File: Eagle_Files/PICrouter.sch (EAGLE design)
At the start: 44 parts, among them IC1 PIC32MX675F512H, IC2 48M033F, J1 POWER_JACK, Q1 20MHz, Q2 BSS84, X2 USB_B

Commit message: Released PICrouter schematic and board v0.4.
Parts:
- added C14, C16, C17, C18, C20, C21, C22, C23, C24: (no value), rcl:C-EUC2012
- added C15, C19: 10uF, rcl:CPOL-USC
- added IC3: DP83848, national-semiconductor:DP83848
- added J2: (no value), pulse_j0011:J0011
- added QG1: SM77H, crystal:SM77H
- added R11, R12, R13, R14: 49.9, SparkFun:RESISTOR0603-RES
- added R15: 4.87k, SparkFun:RESISTOR0603-RES
- added R16, R17, R22: 2.2k, SparkFun:RESISTOR0603-RES
- added R18, R19, R2, R20, R23, R24: 33, SparkFun:RESISTOR0603-RES
- added R21, R25: 1.5k, SparkFun:RESISTOR0603-RES
- added R26, R27: 330, SparkFun:RESISTOR0603-RES
- Q1: device special:XTAL/S -> crystal:CRYSTALCTS406
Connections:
- new net ECRSDV: IC1.ERXDV/ECRSDV/PMD2/RE2, IC3.CRS
- new net EINT: IC1.ECRS/AEREFCLK/IC4/PMCS1/PMA14/INT4/RD11, IC3.PWRDN_INTN, R21.1
- new net EMDC: IC1.AN15/EMDC/AEMDC/OCFB/PMALL/PMA0/CN12/RB15, IC3.MDC
- new net EMDIO: IC1.EMDIO/AEMDIO/SCK3/U4TX/U1RTS/OC2/RD1, IC3.MDIO, R25.2
- new net EREFCLK: IC1.ERXCLK/EREFCLK/PMD3RE3, IC3.X1, R2.2
- new net ERXD0: IC1.ERXD0/PMD1/RE1, R23.1
- new net ERXD1: IC1.ERXD1/PMD0/RE0, R24.1
- new net ERXERR: IC1.ERXERR/PMD4/RE4, IC3.RX_ER
- new net ETXD0: IC1.ETXD0/PMD6/RE6, R19.1
- new net ETXD1: IC1.ETXD1/PMD7/RE7, R20.1
- new net ETXEN: IC1.ETXEN/PMD5/RE5, R18.1
- new net LED_ACT: IC3.LED_ACTCOL, R27.1
- new net LED_LINK: IC3.LED_LNK, R26.1
- new net N$47: IC3.IP_PH_P, R16.1
- new net N$48: IC3.IP_PH_M, R17.1
- new net N$49: IC3.RX_DV, R22.2
- new net N$52: IC3.TXD_1, R20.2
- new net N$53: IC3.TXD_0, R19.2
- new net N$54: IC3.TX_EN, R18.2
- new net N$55: J2.LA, R26.2
- new net N$56: IC3.RXD_0, R23.2
- new net N$57: IC3.RXD_1, R24.2
- new net N$58: QG1.OUT, R2.1
- new net N$62: J2.RA, R27.2
- new net N$9: IC3.VREF, R15.1
- new net PFBOUT: C14.1, C18.1, C19.+, C20.1, IC3.ANA18VDD, IC3.CORE_VDD, IC3.REG_OUT
- new net RDM: IC3.TPRDM, J2.RD-, R11.1
- new net RDP: IC3.TPRDP, J2.RD+, R12.1
- new net TDM: IC3.TPTDM, J2.TD-, R13.1
- new net TDP: IC3.TPTDP, J2.TD+, R14.1
- net GND: now also C14.2, C15.-, C16.2, C17.2, C18.2, C19.-, C20.2, C21.2, C22.2, C23.2, C24.2, IC3.ANA18VSS, IC3.CDVSS, IC3.CORE_VSS, IC3.IO_VSS1, IC3.IO_VSS2, IC3.TXD_3, J2.CGND, J2.LC, J2.RC, J2.S1, J2.S2, QG1.GND, R15.2
- net N$17: now also IC1.ECOL/AECRSDV/SCL1/IC3/PMCS2/PMA15/INT3/RD10; no longer IC1.AN15/EMDC/AEMDC/OCFB/PMALL/PMA0/CN12/RB15
- net VDD: now also C15.+, C16.1, C17.1, C21.1, C22.1, C23.1, C24.1, IC3.ANA33VDD, IC3.IO_VDD1, IC3.IO_VDD2, J2.RCT, J2.TCT, QG1.VCC, R11.2, R12.2, R13.2, R14.2, R16.2, R17.2, R21.2, R22.1, R25.1
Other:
- note added: "03/24/2012"
- note added: "PICrouter v0.5"
- note removed: "09/06/2011"
- note removed: "PICrouter v0.3"

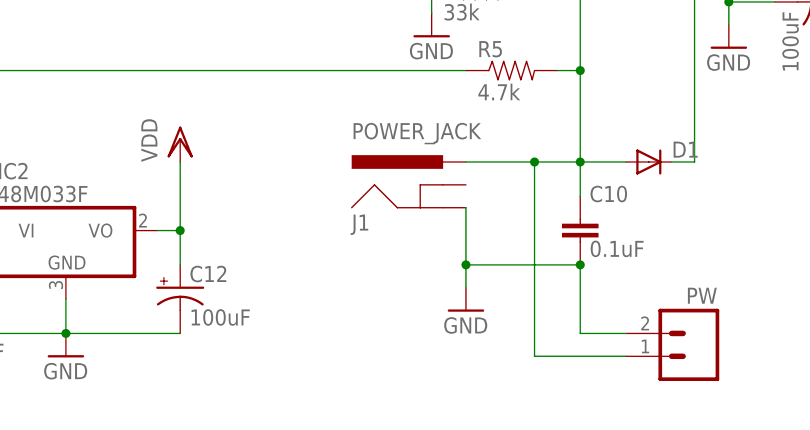
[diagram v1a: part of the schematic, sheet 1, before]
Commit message: Released PICrouter schematic and board v0.6.
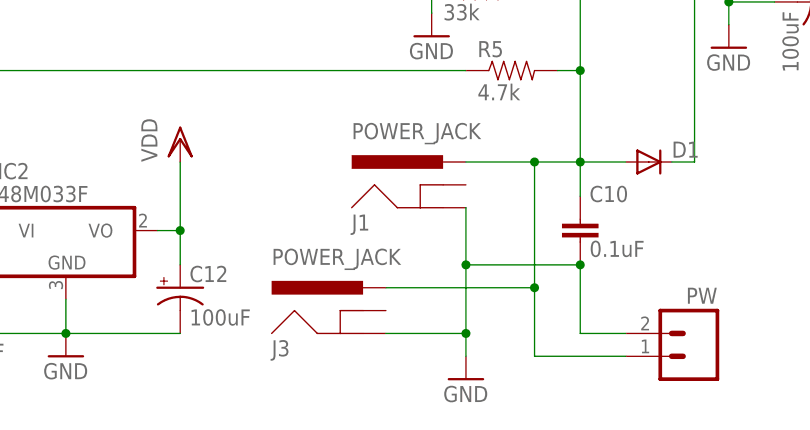
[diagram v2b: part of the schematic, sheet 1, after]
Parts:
- added J3: POWER_JACK, SparkFun:POWER_JACKPTH_LOCK
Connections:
- net GND: now also J3.GND
- net N$46: now also J3.PWR
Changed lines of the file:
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@@
 <part name="R26" library="SparkFun" deviceset="RESISTOR" device="0603-RES" value="330"/>
 <part name="R27" library="SparkFun" deviceset="RESISTOR" device="0603-RES" value="330"/>
+<part name="J3" library="SparkFun" deviceset="POWER_JACK" device="PTH_LOCK" value="POWER_JACK"/>
 </parts>
 <sheets>
@@
 </instance>
 <instance part="C13" gate="G$1" x="199.39" y="49.53" rot="R270"/>
-<instance part="GND10" gate="1" x="160.02" y="15.24"/>
+<instance part="GND10" gate="1" x="160.02" y="7.62"/>
 <instance part="D1" gate="G$1" x="180.34" y="31.75"/>
 <instance part="D2" gate="G$1" x="180.34" y="58.42"/>
@@
 <instance part="C9" gate="G$1" x="207.01" y="133.35"/>
 <instance part="GND19" gate="1" x="212.09" y="138.43" rot="R90"/>
+<instance part="J3" gate="G$1" x="148.59" y="10.16"/>
 </instances>
 <busses>
@@
 <segment>
 <wire x1="160.02" y1="26.67" x2="160.02" y2="20.32" width="0.1524" layer="91"/>
-<wire x1="160.02" y1="20.32" x2="160.02" y2="17.78" width="0.1524" layer="91"/>
+<wire x1="160.02" y1="20.32" x2="160.02" y2="12.7" width="0.1524" layer="91"/>
+<wire x1="160.02" y1="12.7" x2="160.02" y2="10.16" width="0.1524" layer="91"/>
 <wire x1="172.72" y1="20.32" x2="160.02" y2="20.32" width="0.1524" layer="91"/>
 <wire x1="177.8" y1="12.7" x2="172.72" y2="12.7" width="0.1524" layer="91"/>
@@
 <pinref part="C10" gate="G$1" pin="2"/>
 <pinref part="PW" gate="G$1" pin="2"/>
+<pinref part="J3" gate="G$1" pin="GND"/>
+<wire x1="151.13" y1="12.7" x2="160.02" y2="12.7" width="0.1524" layer="91"/>
+<junction x="160.02" y="12.7"/>
 </segment>
 <segment>
@@
 <segment>
 <wire x1="177.8" y1="10.16" x2="167.64" y2="10.16" width="0.1524" layer="91"/>
-<wire x1="167.64" y1="10.16" x2="167.64" y2="31.75" width="0.1524" layer="91"/>
+<wire x1="167.64" y1="10.16" x2="167.64" y2="17.78" width="0.1524" layer="91"/>
+<wire x1="167.64" y1="17.78" x2="167.64" y2="31.75" width="0.1524" layer="91"/>
 <wire x1="166.37" y1="50.8" x2="167.64" y2="50.8" width="0.1524" layer="91"/>
 <wire x1="167.64" y1="50.8" x2="167.64" y2="53.34" width="0.1524" layer="91"/>
@@
 <pinref part="J1" gate="G$1" pin="PWR"/>
 <pinref part="R5" gate="G$1" pin="2"/>
-</segment>
-</net>
+<pinref part="J3" gate="G$1" pin="PWR"/>
+<wire x1="151.13" y1="17.78" x2="167.64" y2="17.78" width="0.1524" layer="91"/>
+<junction x="167.64" y="17.78"/>
+</segment>
+</net>

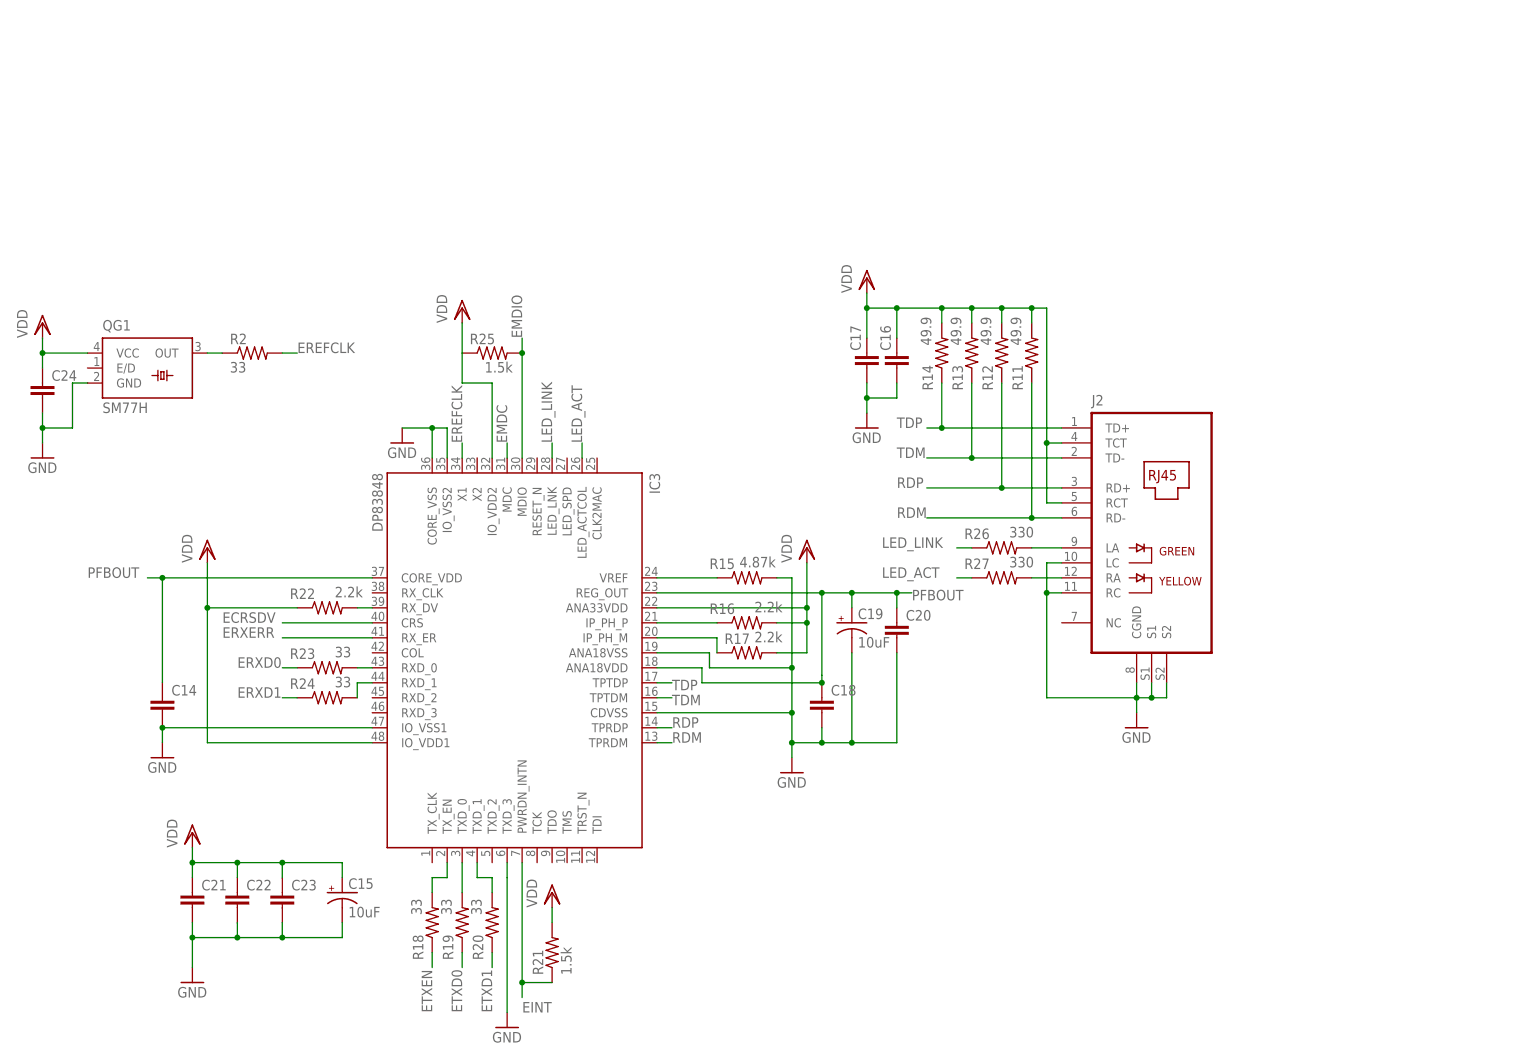
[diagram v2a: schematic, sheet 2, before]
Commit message: Released PICrouter schematic and board v0.7.
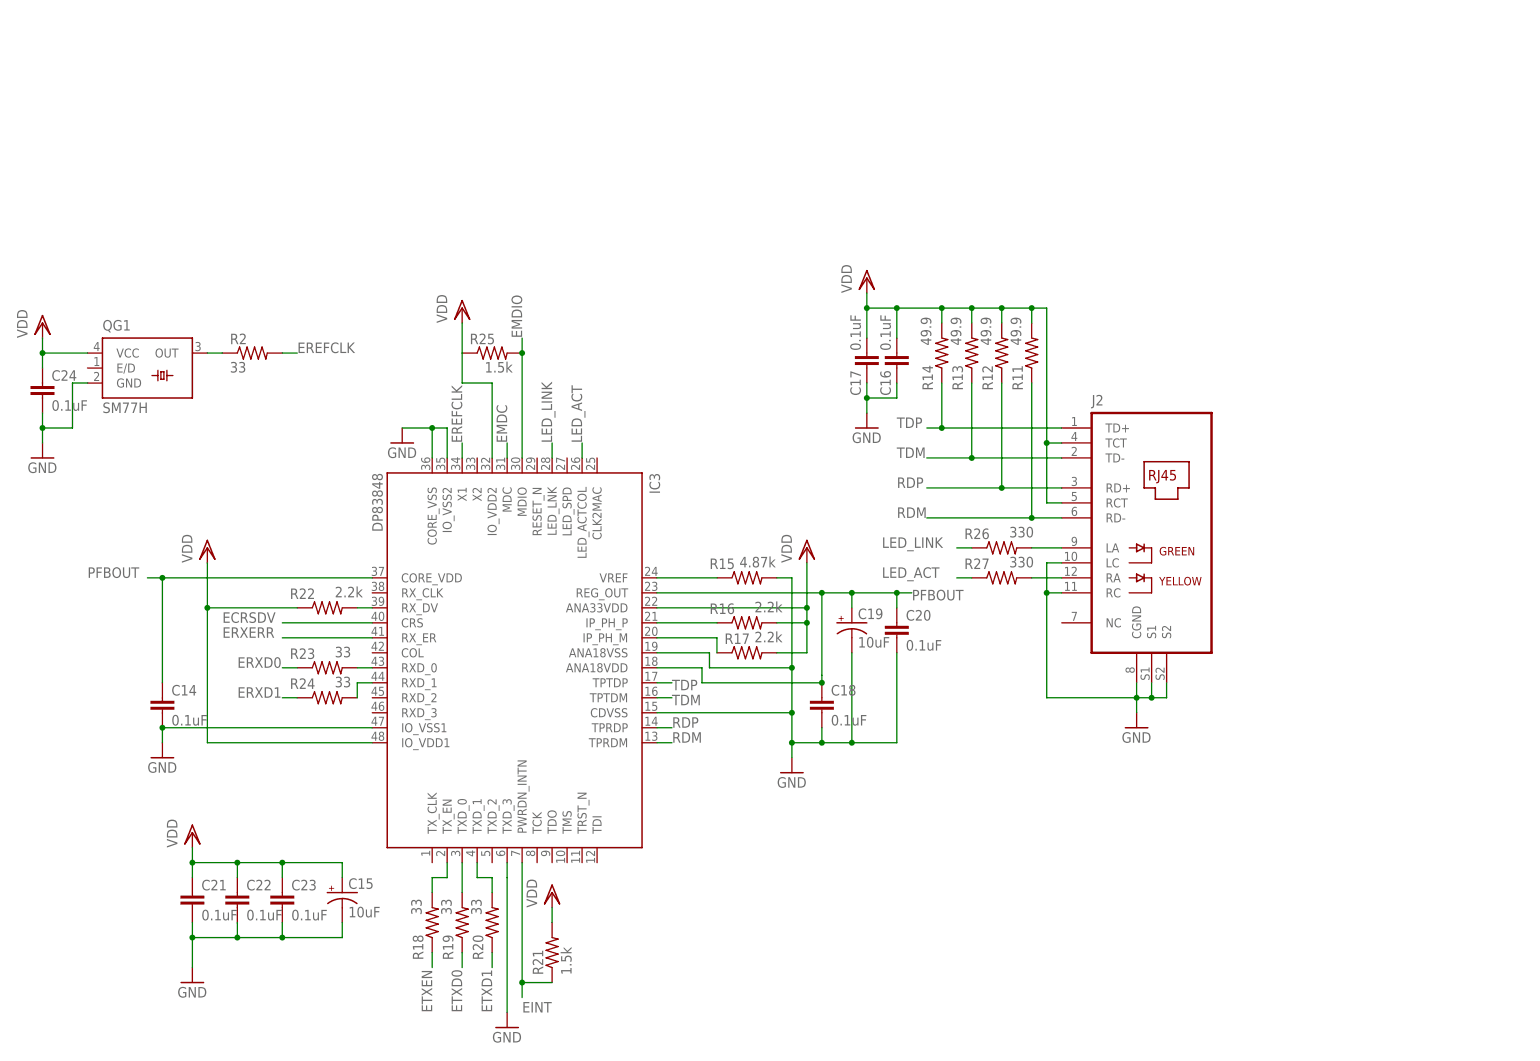
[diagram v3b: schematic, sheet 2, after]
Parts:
- C14, C16, C17, C18, C20, C21, C22, C23, C24: value (none) -> 0.1uF
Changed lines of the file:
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@@
 <setting verticaltext="up"/>
 </settings>
-<grid distance="0.05" unitdist="inch" unit="inch" style="lines" multiple="1" display="no" altdistance="0.01" altunitdist="inch" altunit="inch"/>
+<grid distance="0.1" unitdist="inch" unit="inch" style="lines" multiple="1" display="no" altdistance="0.01" altunitdist="inch" altunit="inch"/>
 <layers>
 <layer number="1" name="Top" color="4" fill="1" visible="no" active="no"/>
@@
 <part name="VDD10" library="supply1" deviceset="VDD" device=""/>
 <part name="GND20" library="supply1" deviceset="GND" device=""/>
-<part name="C14" library="rcl" deviceset="C-EU" device="C2012"/>
+<part name="C14" library="rcl" deviceset="C-EU" device="C2012" value="0.1uF"/>
 <part name="C15" library="rcl" deviceset="CPOL-US" device="C" value="10uF"/>
 <part name="J2" library="pulse_j0011" deviceset="J0011" device=""/>
@@
 <part name="R14" library="SparkFun" deviceset="RESISTOR" device="0603-RES" value="49.9"/>
 <part name="VDD11" library="supply1" deviceset="VDD" device=""/>
-<part name="C16" library="rcl" deviceset="C-EU" device="C2012"/>
-<part name="C17" library="rcl" deviceset="C-EU" device="C2012"/>
+<part name="C16" library="rcl" deviceset="C-EU" device="C2012" value="0.1uF"/>
+<part name="C17" library="rcl" deviceset="C-EU" device="C2012" value="0.1uF"/>
 <part name="GND21" library="supply1" deviceset="GND" device=""/>
 <part name="GND22" library="supply1" deviceset="GND" device=""/>
@@
 <part name="GND23" library="supply1" deviceset="GND" device=""/>
 <part name="VDD12" library="supply1" deviceset="VDD" device=""/>
-<part name="C18" library="rcl" deviceset="C-EU" device="C2012"/>
+<part name="C18" library="rcl" deviceset="C-EU" device="C2012" value="0.1uF"/>
 <part name="C19" library="rcl" deviceset="CPOL-US" device="C" value="10uF"/>
-<part name="C20" library="rcl" deviceset="C-EU" device="C2012"/>
+<part name="C20" library="rcl" deviceset="C-EU" device="C2012" value="0.1uF"/>
 <part name="R18" library="SparkFun" deviceset="RESISTOR" device="0603-RES" value="33"/>
 <part name="R19" library="SparkFun" deviceset="RESISTOR" device="0603-RES" value="33"/>
@@
 <part name="VDD14" library="supply1" deviceset="VDD" device=""/>
 <part name="GND25" library="supply1" deviceset="GND" device=""/>
-<part name="C21" library="rcl" deviceset="C-EU" device="C2012"/>
-<part name="C22" library="rcl" deviceset="C-EU" device="C2012"/>
-<part name="C23" library="rcl" deviceset="C-EU" device="C2012"/>
+<part name="C21" library="rcl" deviceset="C-EU" device="C2012" value="0.1uF"/>
+<part name="C22" library="rcl" deviceset="C-EU" device="C2012" value="0.1uF"/>
+<part name="C23" library="rcl" deviceset="C-EU" device="C2012" value="0.1uF"/>
 <part name="VDD15" library="supply1" deviceset="VDD" device=""/>
 <part name="GND26" library="supply1" deviceset="GND" device=""/>
@@
 <part name="GND27" library="supply1" deviceset="GND" device=""/>
 <part name="VDD16" library="supply1" deviceset="VDD" device=""/>
-<part name="C24" library="rcl" deviceset="C-EU" device="C2012"/>
+<part name="C24" library="rcl" deviceset="C-EU" device="C2012" value="0.1uF"/>
 <part name="R26" library="SparkFun" deviceset="RESISTOR" device="0603-RES" value="330"/>
 <part name="R27" library="SparkFun" deviceset="RESISTOR" device="0603-RES" value="330"/>
@@
 <instance part="VDD11" gate="G$1" x="119.38" y="101.6"/>
 <instance part="C16" gate="G$1" x="124.46" y="88.9" smashed="yes">
-<attribute name="NAME" x="123.444" y="89.281" size="1.778" layer="95" rot="R90"/>
-<attribute name="VALUE" x="125.984" y="84.201" size="1.778" layer="96"/>
+<attribute name="NAME" x="123.444" y="81.661" size="1.778" layer="95" rot="R90"/>
+<attribute name="VALUE" x="123.444" y="89.281" size="1.778" layer="96" rot="R90"/>
 </instance>
 <instance part="C17" gate="G$1" x="119.38" y="88.9" smashed="yes">
-<attribute name="NAME" x="118.364" y="89.281" size="1.778" layer="95" rot="R90"/>
-<attribute name="VALUE" x="120.904" y="84.201" size="1.778" layer="96"/>
+<attribute name="NAME" x="118.364" y="81.661" size="1.778" layer="95" rot="R90"/>
+<attribute name="VALUE" x="118.364" y="89.281" size="1.778" layer="96" rot="R90"/>
 </instance>
 <instance part="GND21" gate="1" x="119.38" y="76.2"/>

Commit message: Released PICrouter schematic and board v0.71.
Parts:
- removed J1: POWER_JACK, SparkFun:POWER_JACKPTH_LOCK
- removed X2: USB_B, con-cypressindustries:MINI-USB_4P-85-32004-10X
- added C25: 100uF, rcl:CPOL-USC
- added C26: 0.1uF, rcl:C-EUC2012
- added F1: PTCSMD, SparkFun:PTCSMD
- added U1: USB+SHIELD, SparkFun:USB+SHIELD
- added X1: USB-A-H, SparkFun:USB-A-H
- IC1: device PIC:PIC32MX675F512H -> PIC.rpt:PIC32MX675F512H
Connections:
- removed net N$61: C13.+, C9.2, IC1.VBUS, Q2.S, R4.1, R6.2, X2.1
- new net N$50: C13.+, C25.+, C9.2, F1.1, IC1.VBUS, Q2.S, R4.1, R6.2, U1.VBUS, X1.GND
- net GND: now also C25.-, C26.2, IC1.GND, IC1.GND@1, IC1.GND@2, U1.GND, U1.P$1, U1.P$2, X1.S1, X1.S2, X1.VBUS; no longer IC1.VSS, IC1.VSS@1, IC1.VSS@2, J1.GND, X2.4
- net N$45: now also U1.D-, X1.D+; no longer X2.2
- net N$46: no longer J1.PWR
- net N$5: now also U1.D+, X1.D-; no longer X2.3
- net VCC: now also F1.2
- net VDD: now also C26.1
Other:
- note added: "03/29/2012"
- note added: "PICrouter v0.7"
- note added: "USB Device"
- note added: "USB Host"
- note removed: "03/24/2012"
- note removed: "PICrouter v0.5"
- moved on the sheet: 3.3V, 5V, C1, C12, C14, C15, C16, C17, C18, C19, C2, C20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

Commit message: Released PICrouter schematic and board v0.8.
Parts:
- AN: value AN -> M14
- C13: value 100uF -> 10uF
- C25: value 100uF -> 150uF
- I/O: value I/O -> (none)
- OC: value OC -> (none)
- SPI2: value SPI2 -> (none)
- SPI4: value SPI4 -> (none)
- U1: value USB+SHIELD -> DEVICE
- renumbered JP1 to ICSP, JP2 to SPI2, JP3 to SPI4, JP4 to AN, JP5 to OC, JP6 to I/O
